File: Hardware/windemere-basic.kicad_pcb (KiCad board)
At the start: 2 copper layers, 152.4 x 158.8 mm, 67 parts, among them J3 Connector, J6 Barrel_Jack, SW1 Reset Button, U1 HD44780U, U2 WD65C02, U3 28C256, U4 62256, U5 WD65C22, U6 74HC00, U7 MM74C922, U8 L7805, U9 MCP102-475, X1 1MHz

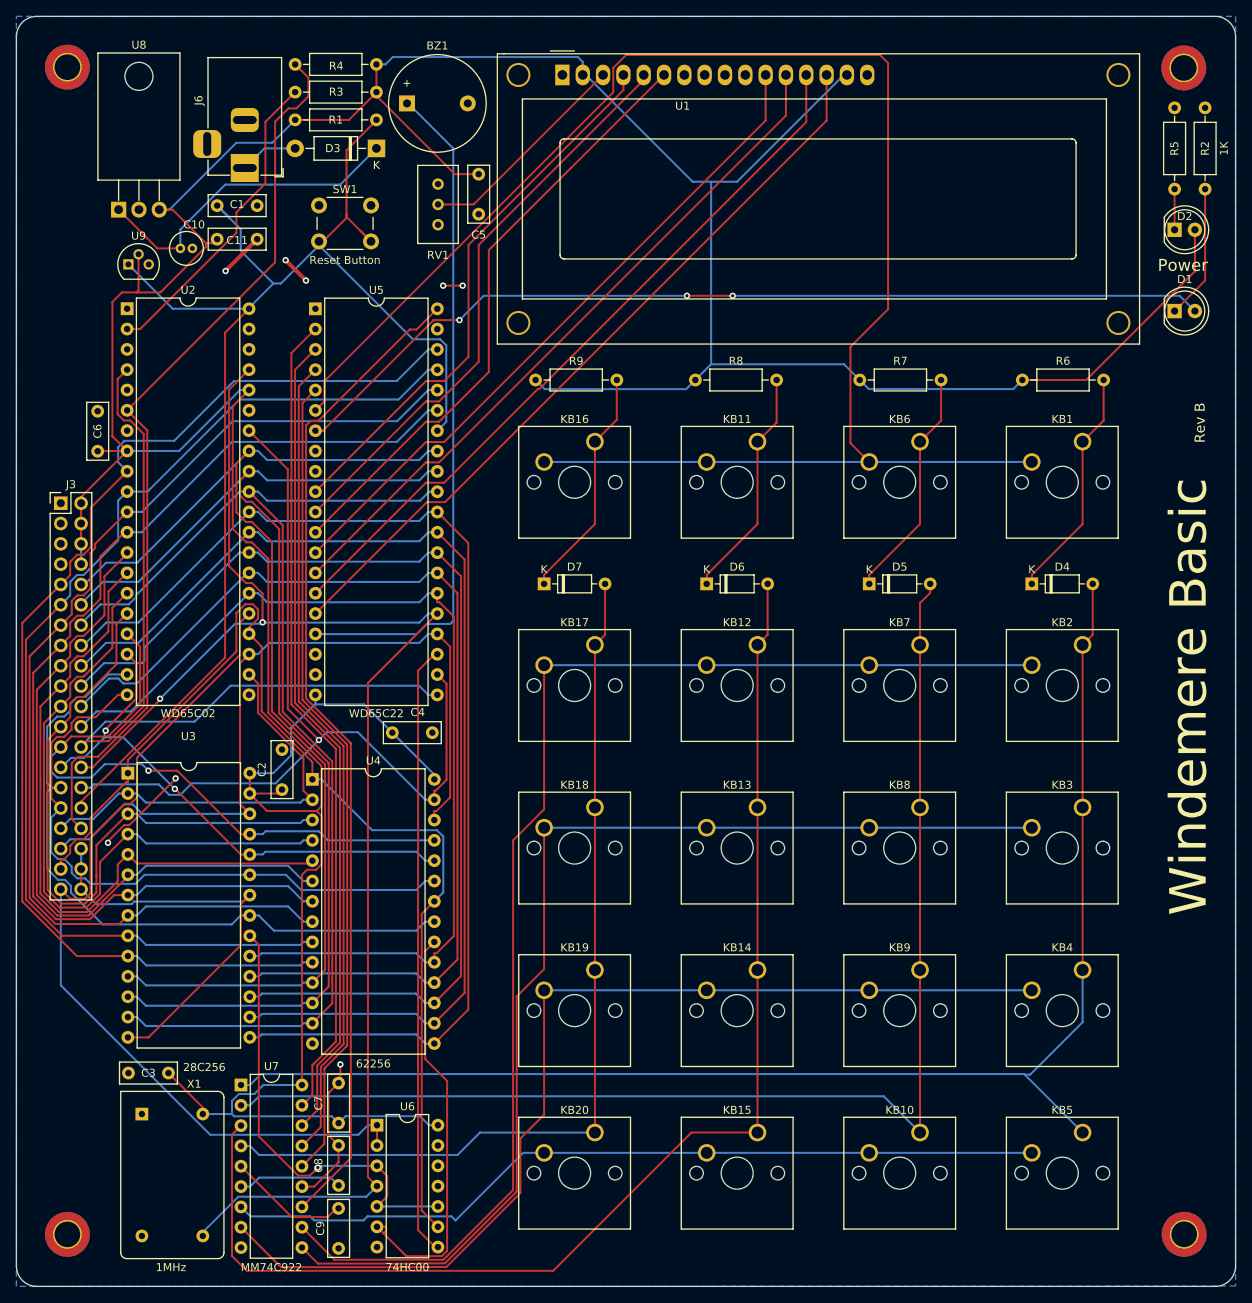
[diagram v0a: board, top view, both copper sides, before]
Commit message: Hardware: Change from 74HC00 to 74LS00
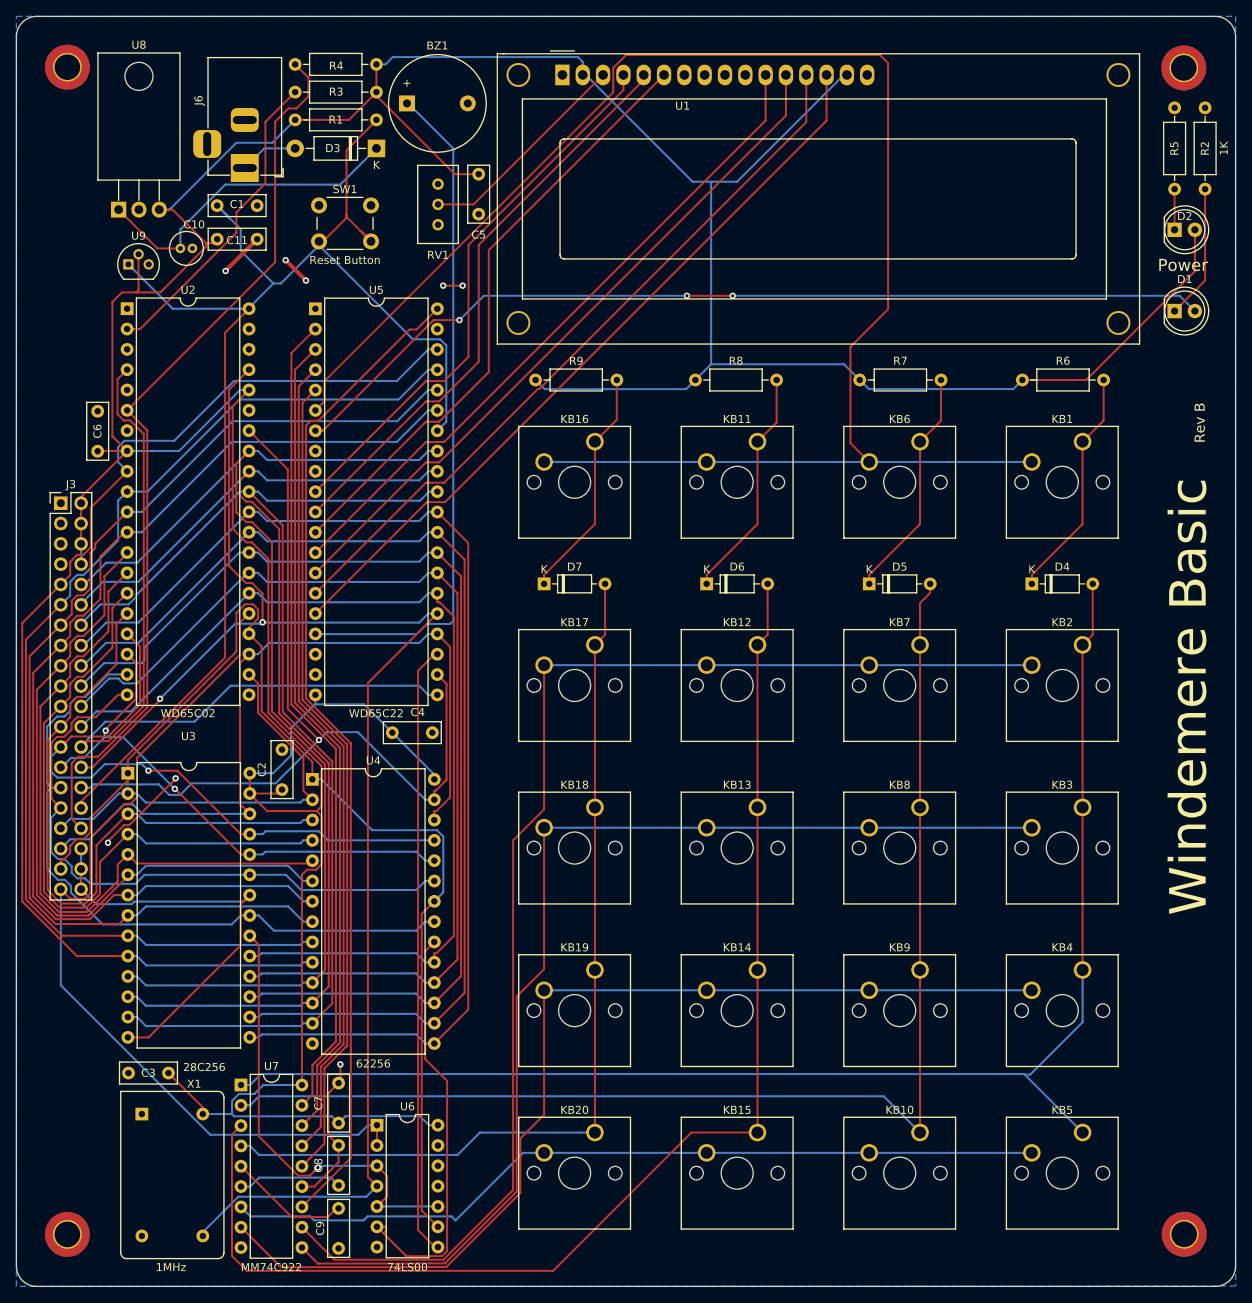
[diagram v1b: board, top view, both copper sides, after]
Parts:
- U6: value 74HC00 -> 74LS00
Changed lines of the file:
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@@
         (effects (font (size 1 1) (thickness 0.15)))
     )
-    (fp_text value "74HC00" (at 3.81 17.7758) (layer "F.SilkS")
+    (fp_text value "74LS00" (at 3.81 17.7758) (layer "F.SilkS")
         (effects (font (size 1 1) (thickness 0.15)))
     )
@@
     (fp_arc (start 63.7 8) (mid 64.053553 8.146447) (end 64.2 8.5)
       (stroke (width 0.12) (type solid)) (layer "F.SilkS"))
-    (fp_arc (start 64.20104 22.49932) (mid 64.054479 22.85315) (end 63.70066 22.9997)
+    (fp_arc (start 64.20104 22.49932) (mid 64.054473 22.853115) (end 63.70066 22.9997)
       (stroke (width 0.12) (type solid)) (layer "F.SilkS"))
     (fp_line (start -8.25 -2.75) (end -8.25 33.75)

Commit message: Change to MM74LS923
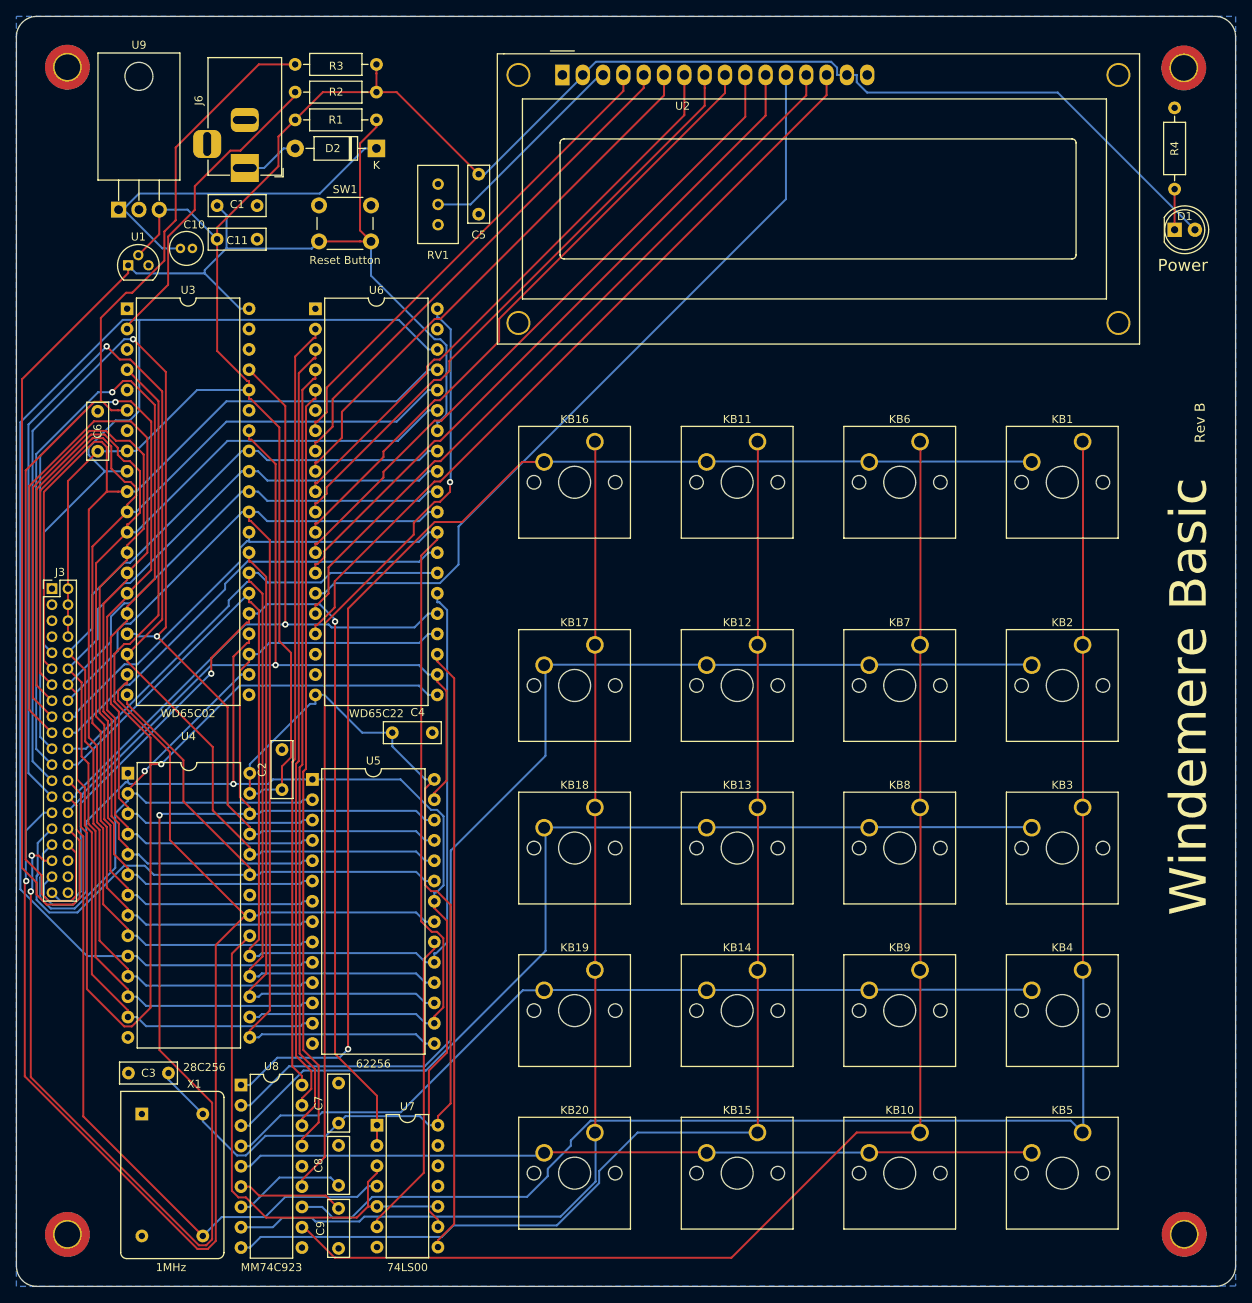
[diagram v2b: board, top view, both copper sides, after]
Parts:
- removed BZ1: Buzzer, Buzzer_Beeper:Buzzer_12x9.5RM7.6
- removed the D1 at (278.1, 69.5)
- removed D4, D5, D6, D7: 1N914, Diode_THT:D_DO-35_SOD27_P7.62mm_Horizontal
- removed the R2 at (282.0, 54.2)
- removed R6, R7, R8, R9: 100K, Resistor_THT:R_Axial_DIN0207_L6.3mm_D2.5mm_P10.16mm_Horizontal
- removed the U9 at (147.4, 63.6)
- added U1: MCP102-475, Package_TO_SOT_THT:TO-92, F.Cu at (147.3, 63.7)
- J3: footprint Connector_PinHeader_2.54mm:PinHeader_2x20_P2.54mm_Vertical -> Connector_PinHeader_2.00mm:PinHeader_2x20_P2.00mm_Vertical
- U8: renamed from U7; value MM74C922 -> MM74C923
- moved J3 10.7 mm to (137.8, 104.2)
- renumbered D2 to D1, D3 to D2, R3 to R2, R4 to R3, R5 to R4, U1 to U2, U2 to U3, U3 to U4, U4 to U5, U5 to U6, U6 to U7, U8 to U9
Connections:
- C8 pad 1: Net-(U7-KBM) -> Net-(U8-KBM)
- C9 pad 1: Net-(U7-OSC) -> Net-(U8-OSC)
- KB1 pad 1: Net-(D4-K) -> Net-(U8-X1)
- KB1 pad 2: Net-(U5-PA4) -> Net-(U8-Y1)
- KB10 pad 1: Net-(D5-A) -> Net-(U8-X2)
- KB10 pad 2: Net-(U7-X4) -> Net-(U8-Y5)
- KB11 pad 1: Net-(D6-K) -> Net-(U8-X3)
- KB11 pad 2: Net-(U5-PA4) -> Net-(U8-Y1)
- KB12 pad 1: Net-(D6-A) -> Net-(U8-X3)
- KB12 pad 2: Net-(U7-X1) -> Net-(U8-Y2)
- KB13 pad 1: Net-(D6-A) -> Net-(U8-X3)
- KB13 pad 2: Net-(U7-X2) -> Net-(U8-Y3)
- KB14 pad 1: Net-(D6-A) -> Net-(U8-X3)
- KB14 pad 2: Net-(U7-X3) -> Net-(U8-Y4)
- KB15 pad 1: Net-(D6-A) -> Net-(U8-X3)
- KB15 pad 2: Net-(U7-X4) -> Net-(U8-Y5)
- KB16 pad 1: Net-(D7-K) -> Net-(U8-X4)
- KB16 pad 2: Net-(U5-PA4) -> Net-(U8-Y1)
- KB17 pad 1: Net-(D7-A) -> Net-(U8-X4)
- KB17 pad 2: Net-(U7-X1) -> Net-(U8-Y2)
- KB18 pad 1: Net-(D7-A) -> Net-(U8-X4)
- KB18 pad 2: Net-(U7-X2) -> Net-(U8-Y3)
- KB19 pad 1: Net-(D7-A) -> Net-(U8-X4)
- KB19 pad 2: Net-(U7-X3) -> Net-(U8-Y4)
- KB2 pad 1: Net-(D4-A) -> Net-(U8-X1)
- KB2 pad 2: Net-(U7-X1) -> Net-(U8-Y2)
- KB20 pad 1: Net-(D7-A) -> Net-(U8-X4)
- KB20 pad 2: Net-(U7-X4) -> Net-(U8-Y5)
- KB3 pad 1: Net-(D4-A) -> Net-(U8-X1)
- KB3 pad 2: Net-(U7-X2) -> Net-(U8-Y3)
- KB4 pad 1: Net-(D4-A) -> Net-(U8-X1)
- KB4 pad 2: Net-(U7-X3) -> Net-(U8-Y4)
- KB5 pad 1: Net-(D4-A) -> Net-(U8-X1)
- KB5 pad 2: Net-(U7-X4) -> Net-(U8-Y5)
- KB6 pad 1: Net-(D5-K) -> Net-(U8-X2)
- KB6 pad 2: Net-(U5-PA4) -> Net-(U8-Y1)
- KB7 pad 1: Net-(D5-A) -> Net-(U8-X2)
- KB7 pad 2: Net-(U7-X1) -> Net-(U8-Y2)
- KB8 pad 1: Net-(D5-A) -> Net-(U8-X2)
- KB8 pad 2: Net-(U7-X2) -> Net-(U8-Y3)
- KB9 pad 1: Net-(D5-A) -> Net-(U8-X2)
- KB9 pad 2: Net-(U7-X3) -> Net-(U8-Y4)
- U2 pad 10: GND -> Net-(U2-DB3)
- U2 pad 11: Net-(U1-DB4) -> Net-(U2-DB4)
- U2 pad 12: Net-(U1-DB5) -> Net-(U2-DB5)
- U2 pad 13: Net-(U1-DB6) -> Net-(U2-DB6)
- U2 pad 14: Net-(U1-DB7) -> Net-(U2-DB7)
- U2 pad 4: Net-(U1-RS) -> Net-(U2-RS)
- U2 pad 5: Net-(U1-R/~{W}) -> Net-(U2-R/~{W})
- U2 pad 6: Net-(U1-E) -> Net-(U2-E)
- U2 pad 7: GND -> Net-(U2-DB0)
- U2 pad 8: GND -> Net-(U2-DB1)
- U2 pad 9: GND -> Net-(U2-DB2)
- U6 pad 10: Net-(U1-RS) -> Net-(U2-DB0)
- U6 pad 11: Net-(U1-R/~{W}) -> Net-(U2-DB1)
- U6 pad 12: Net-(U1-E) -> Net-(U2-DB2)
- U6 pad 13: Net-(U1-DB4) -> Net-(U2-DB3)
- U6 pad 14: Net-(U1-DB5) -> Net-(U2-DB4)
- U6 pad 15: Net-(U1-DB6) -> Net-(U2-DB5)
- U6 pad 16: Net-(U1-DB7) -> Net-(U2-DB6)
- U6 pad 17: Net-(BZ1--) -> Net-(U2-DB7)
- U6 pad 2: Net-(U5-PA0) -> Net-(U6-PA0)
- U6 pad 3: Net-(U5-PA1) -> Net-(U6-PA1)
- U6 pad 4: Net-(U5-PA2) -> Net-(U6-PA2)
- U6 pad 40: Net-(U5-CA1) -> Net-(U6-CA1)
- U6 pad 5: Net-(U5-PA3) -> Net-(U6-PA3)
- U6 pad 6: Net-(U5-PA4) -> Net-(U6-PA4)
- U6 pad 7: Net-(D1-A) -> Net-(U2-RS)
- U6 pad 8: unconnected-(U5-PA6-Pad8) -> Net-(U2-R/~{W})
- U6 pad 9: unconnected-(U5-PA7-Pad9) -> Net-(U2-E)
- U8 pad 1: Net-(D4-A) -> Net-(U8-Y1)
- U8 pad 10: Net-(U7-X2) -> GND
- U8 pad 11: Net-(U7-X1) -> Net-(U8-X2)
- U8 pad 12: Net-(U5-CA1) -> Net-(U8-X1)
- U8 pad 13: GND -> Net-(U6-CA1)
- U8 pad 14: Net-(U5-PA3) -> GND
- U8 pad 15: Net-(U5-PA2) -> Net-(U6-PA3)
- U8 pad 16: Net-(U5-PA1) -> Net-(U6-PA2)
- U8 pad 17: Net-(U5-PA0) -> Net-(U6-PA1)
- U8 pad 18: +5V -> Net-(U6-PA0)
- U8 pad 2: Net-(D5-A) -> Net-(U8-Y2)
- U8 pad 3: Net-(D6-A) -> Net-(U8-Y3)
- U8 pad 4: Net-(D7-A) -> Net-(U8-Y4)
- U8 pad 5: Net-(U7-OSC) -> Net-(U8-Y5)
- U8 pad 6: Net-(U7-KBM) -> Net-(U8-OSC)
- U8 pad 7: Net-(U7-X4) -> Net-(U8-KBM)
- U8 pad 8: Net-(U7-X3) -> Net-(U8-X4)
- U8 pad 9: GND -> Net-(U8-X3)
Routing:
- net Net-(U5-PA4): track 207.4 -> 0.00 mm
- net Net-(U8-X1): track 0.00 -> 191.3 mm
- net Net-(D4-A): track 174.1 -> 0.00 mm
- net Net-(U8-X2): track 0.00 -> 171.8 mm
- net Net-(U8-Y1): track 0.00 -> 163.5 mm, vias 0 -> 1
- net Net-(U7-X1): track 159.9 -> 0.00 mm
- net Net-(D6-A): track 159.5 -> 0.00 mm
- net Net-(U8-X3): track 0.00 -> 157.9 mm
- net Net-(D5-A): track 156.3 -> 0.00 mm
- net Net-(U8-Y2): track 0.00 -> 142.4 mm
- net Net-(U8-X4): track 0.00 -> 139.7 mm
- net Net-(U7-X2): track 139.3 -> 0.00 mm
- net Net-(U7-X3): track 128.4 -> 0.00 mm
- net Net-(U5-CA1): track 125.0 -> 0.00 mm
- net Net-(U8-Y3): track 0.00 -> 123.7 mm
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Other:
- board text added: "©2021 by Matt Rude <matt@mattrude.com> https://github.com/mattrude/windemere-basic Designed and engineered in Windemere Township, Pine County, Minnesota, USA"
- board text removed: "©2022 by Matt Rude <matt@mattrude.com> https://github.com/mattrude/windemere-basic"

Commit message: Update windemere-basic.kicad_pcb
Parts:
- moved R4 107.4 mm to (172.1, 37.1), turned to 0 degrees
- moved D1 93.4 mm to (186.7, 40.2)
- moved C5 27.0 mm to (167.0, 64.4), turned to 180 degrees
- moved D2 4.50 mm to (182.3, 51.4)
- moved R3 4.50 mm to (172.1, 40.9)
- moved R1 4.50 mm to (172.1, 47.8)
- moved R2 4.50 mm to (172.1, 44.3)
- moved C1 3.65 mm to (162.0, 55.3)
- moved C11 3.58 mm to (162.0, 59.8)
- moved U1 2.64 mm to (149.8, 62.8)
- moved C10 2.64 mm to (156.3, 60.7)
- moved U9 2.64 mm to (148.6, 55.8)
- moved J6 2.64 mm to (164.4, 50.6)
- moved SW1 2.57 mm to (173.7, 57.0)
- moved RV1 2.30 mm to (188.0, 57.4)
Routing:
- net +5V: track 420.1 -> 0.00 mm
- net /A0: track 210.4 -> 0.00 mm
- net /A13: track 198.6 -> 0.00 mm, vias 3 -> 0
- net Net-(J3-Pin_32): track 191.5 -> 0.00 mm
- net Net-(U8-X1): track 191.3 -> 0.00 mm
- net Net-(J3-Pin_28): track 176.1 -> 0.00 mm, vias 1 -> 0
- net /A10: track 172.0 -> 0.00 mm, vias 1 -> 0
- net Net-(U8-X2): track 171.8 -> 0.00 mm
- net /A3: track 171.2 -> 0.00 mm
- net /A2: track 170.1 -> 0.00 mm
- net /A1: track 168.6 -> 0.00 mm
- net Net-(J3-Pin_26): track 164.2 -> 0.00 mm, vias 1 -> 0
- net Net-(U8-Y1): track 163.5 -> 0.00 mm, vias 1 -> 0
- net /A9: track 160.6 -> 0.00 mm, vias 1 -> 0
- net /A8: track 158.4 -> 0.00 mm, vias 2 -> 0
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
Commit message: Update windemere-basic.kicad_pcb
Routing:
- net +5V: track 0.00 -> 370.1 mm
- net Net-(J3-Pin_28): track 0.00 -> 300.5 mm
- net /A1: track 0.00 -> 197.8 mm, vias 0 -> 1
- net Net-(U8-X1): track 0.00 -> 190.4 mm
- net Net-(U6-CA1): track 0.00 -> 186.8 mm
- net /A14: track 0.00 -> 173.6 mm
- net Net-(U8-Y1): track 0.00 -> 173.3 mm
- net Net-(U8-X2): track 0.00 -> 172.1 mm
- net Net-(J3-Pin_32): track 0.00 -> 170.4 mm
- net /A0: track 0.00 -> 161.6 mm, vias 0 -> 1
- net /A2: track 0.00 -> 157.6 mm
- net Net-(U8-X3): track 0.00 -> 157.0 mm
- net /D0: track 0.00 -> 155.9 mm
- net Net-(U6-PA3): track 0.00 -> 155.7 mm, vias 0 -> 1
- net /D1: track 0.00 -> 155.3 mm
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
